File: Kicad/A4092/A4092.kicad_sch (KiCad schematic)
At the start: 0 parts

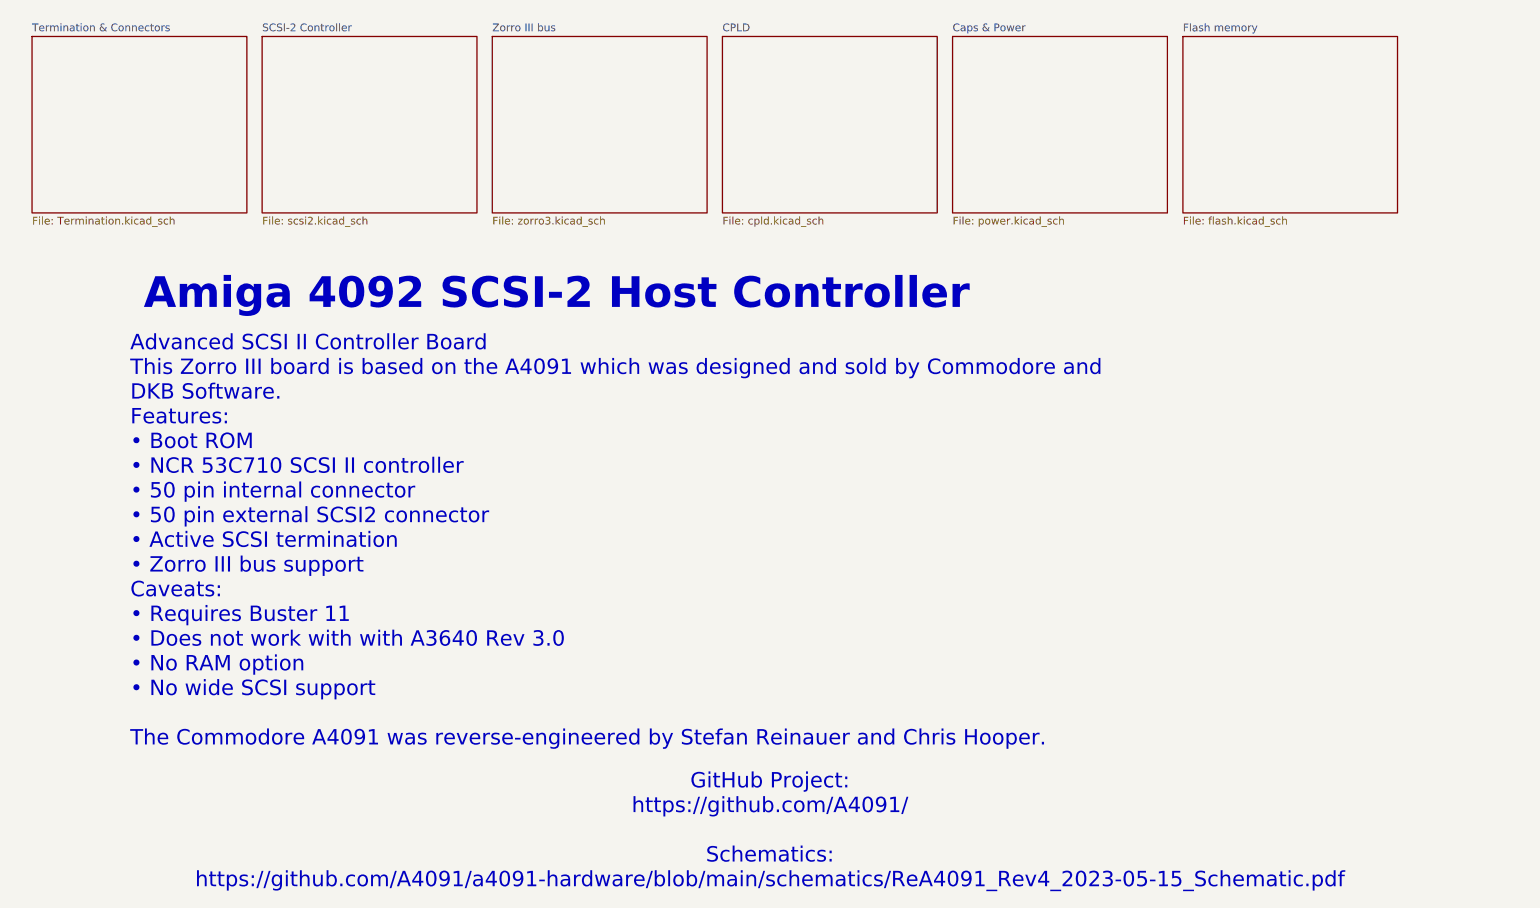
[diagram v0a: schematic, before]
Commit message: A4092 Schematics Revision C
- Power U5 / 74LVC07 from 3.3V rail
- Use ABOEH for 1OEAB on U4 / 74ABT16543
- Add bypass capacitor C501 for U5 / 74LVC07
- Remove EMI filters and capacitors from SCSI lines. They
  are a net negative for signal integrity
- Remove DIP switch circuit as all options are controlled
  by the CPLD / AutoConfig ROM now.
- Remove parallel flash memory, as SPI works reliably and
  is significantly easier to source.
- Remove all ferrite beads from signal lines, as these were
  populated with 0 Ohm resistors in all Proto devices.
- Mark power connector and 12V capacitor as DNP
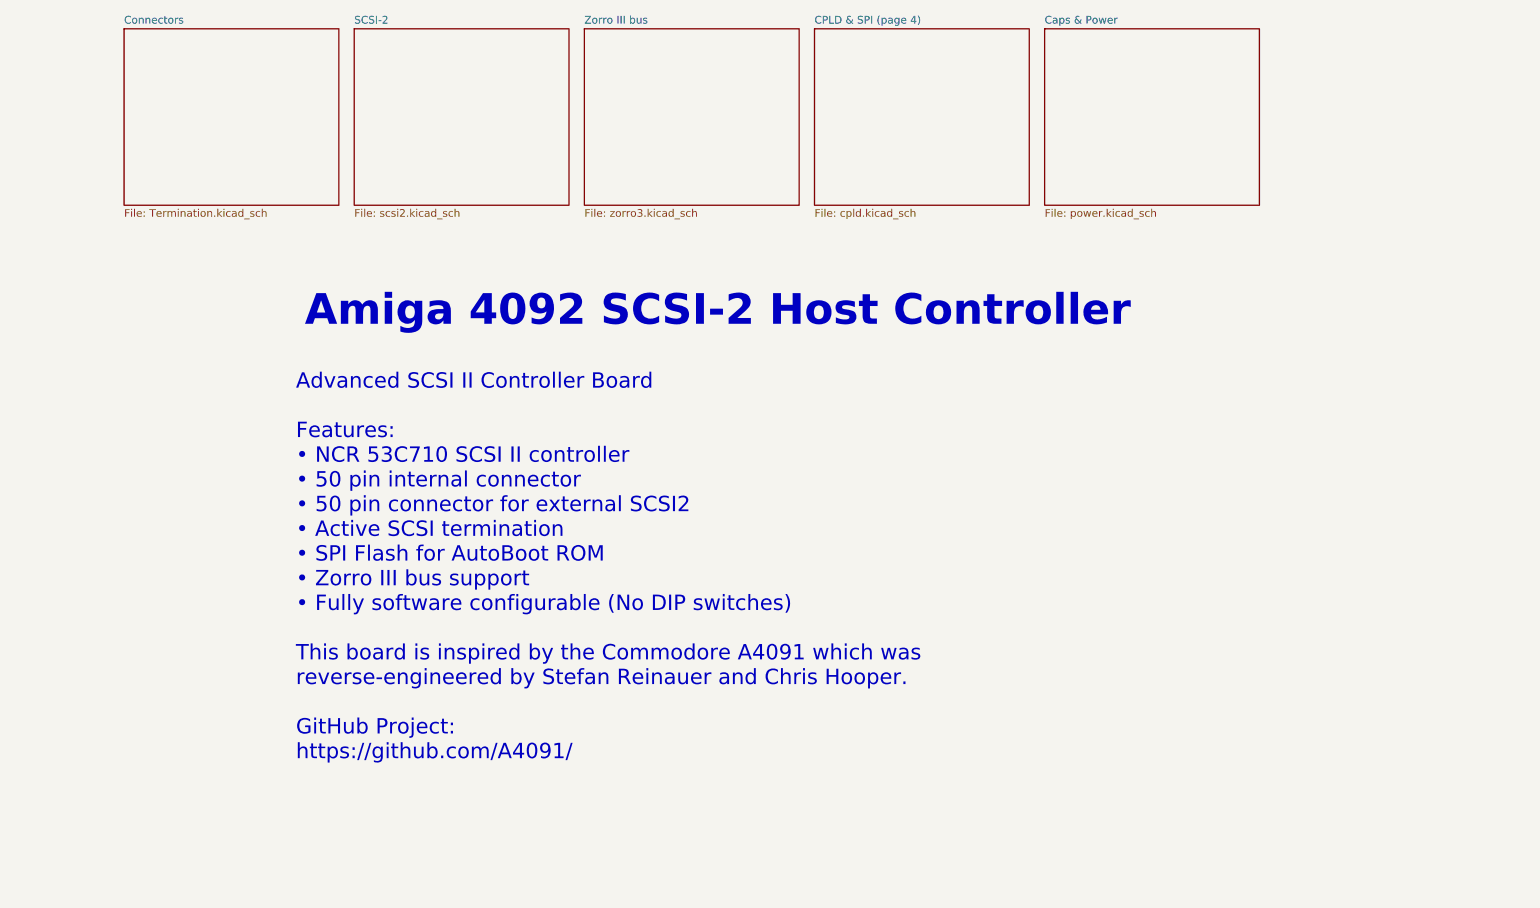
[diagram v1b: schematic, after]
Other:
- sheet CPLD renamed CPLD & SPI (page 4)
- sheet SCSI-2 Controller renamed SCSI-2
- sheet Termination & Connectors renamed Connectors
- removed sheet Flash memory
- note added: "Advanced SCSI II Controller Board Features: • NCR 53C710 SCSI II controller • 50 pin internal connector • 50 pin connector for external SCSI2 • Active SCSI termination • SPI Flash for AutoBoot ROM • Zorro III bus support • Fully software configurable (No DIP switches) This board is inspired by the Commodore A4091 which was reverse-engineered by Stefan Reinauer and Chris Hooper. GitHub Project: ht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"
- note removed: "Advanced SCSI II Controller Board This Zorro III board is based on the A4091 which was designed and sold by Commodore and DKB Software. Features: • Boot ROM • NCR 53C710 SCSI II controller • 50 pin internal connector • 50 pin external SCSI2 connector • Active SCSI termination • Zorro III bus support Caveats: • Requires Buster 11 • Does not work with with A3640 Rev 3.0 • No RAM option • No wide SC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"
- note removed: "GitHub Project: https://github.com/A4091/ Schematics: https://github.com/A4091/a4091-hardware/blob/main/schematics/ReA4091_Rev4_2023-05-15_Schematic.pdf"
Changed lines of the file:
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@@
 	(title_block
 		(title "A4092")
-		(rev "PROTO0")
+		(date "2026-01-08")
+		(rev "REV C")
 		(company "amiga.technology")
 	)
-	(text "Advanced SCSI II Controller Board\nThis Zorro III board is based on the A4091 which was designed and sold by Commodore and\nDKB Software.\nFeatures:\n• Boot ROM\n• NCR 53C710 SCSI II controller\n• 50 pin internal connector\n• 50 pin external SCSI2 connector\n• Active SCSI termination\n• Zorro III bus support\nCaveats:\n• Requires Buster 11\n• Does not work with with A3640 Rev 3.0\n• No RAM option\n• No wide SCSI support\n\nThe Commodore A4091 was reverse-engineered by Stefan Reinauer and Chris Hooper. "
-		(exclude_from_sim no)
-		(at 51.816 105.156 0)
+	(text "Advanced SCSI II Controller Board\n\nFeatures:\n• NCR 53C710 SCSI II controller\n• 50 pin internal connector\n• 50 pin connector for external SCSI2\n• Active SCSI termination\n• SPI Flash for AutoBoot ROM\n• Zorro III bus support\n• Fully software configurable (No DIP switches)\n\nThis board is inspired by the Commodore A4091 which was \nreverse-engineered by Stefan Reinauer and Chris Hooper. \n\nGitHub Project:\nhttps://github.com/A4091/"
+		(exclude_from_sim no)
+		(at 79.248 109.474 0)
 		(effects
 			(font
@@
 		)
 	)
-	(text "GitHub Project:\nhttps://github.com/A4091/\n\nSchematics:\nhttps://github.com/A4091/a4091-hardware/blob/main/schematics/ReA4091_Rev4_2023-05-15_Schematic.pdf"
-		(exclude_from_sim no)
-		(at 157.734 153.162 0)
-		(effects
-			(font
-				(size 2.54 2.54)
-			)
-		)
-	)
 	(text "Amiga 4092 SCSI-2 Host Controller\n"
 		(exclude_from_sim no)
-		(at 122.428 64.262 0)
+		(at 149.098 67.056 0)
 		(effects
 			(font
@@
 	)
 	(sheet
-		(at 187.96 21.59)
+		(at 203.2 20.32)
 		(size 35.56 29.21)
 		(exclude_from_sim no)
@@
 		)
 		(property "Sheetname" "Caps & Power"
-			(at 187.96 20.8784 0)
+			(at 203.2 19.6084 0)
 			(effects
 				(font
@@
 		)
 		(property "Sheetfile" "power.kicad_sch"
-			(at 187.96 51.3846 0)
+			(at 203.2 50.1146 0)
 			(effects
 				(font
@@
 	)
 	(sheet
-		(at 73.66 21.59)
-		(size 35.56 29.21)
-		(exclude_from_sim no)
-		(in_bom yes)
-		(on_board yes)
-		(dnp no)
-		(fields_autoplaced yes)
-		(stroke
-			(width 0.1524)
-			(type solid)
-		)
-		(fill
-			(color 0 0 0 0.0000)
-		)
-		(property "Sheetname" "SCSI-2 Controller"
-			(at 73.66 20.8784 0)
+		(at 88.9 20.32)
+		(size 35.56 29.21)
+		(exclude_from_sim no)
+		(in_bom yes)
+		(on_board yes)
+		(dnp no)
+		(fields_autoplaced yes)
+		(stroke
+			(width 0.1524)
+			(type solid)
+		)
+		(fill
+			(color 0 0 0 0.0000)
+		)
+		(property "Sheetname" "SCSI-2"
+			(at 88.9 19.6084 0)
 			(effects
 				(font
@@
 		)
 		(property "Sheetfile" "scsi2.kicad_sch"
-			(at 73.66 51.3846 0)
+			(at 88.9 50.1146 0)
 			(effects
 				(font
@@
 	)
 	(sheet
-		(at 35.56 21.59)
-		(size 35.56 29.21)
-		(exclude_from_sim no)
-		(in_bom yes)
-		(on_board yes)
-		(dnp no)
-		(fields_autoplaced yes)
-		(stroke
-			(width 0.1524)
-			(type solid)
-		)
-		(fill
-			(color 0 0 0 0.0000)
-		)
-		(property "Sheetname" "Termination & Connectors"
-			(at 35.56 20.8784 0)
+		(at 50.8 20.32)
+		(size 35.56 29.21)
+		(exclude_from_sim no)
+		(in_bom yes)
+		(on_board yes)
+		(dnp no)
+		(fields_autoplaced yes)
+		(stroke
+			(width 0.1524)
+			(type solid)
+		)
+		(fill
+			(color 0 0 0 0.0000)
+		)
+		(property "Sheetname" "Connectors"
+			(at 50.8 19.6084 0)
 			(effects
 				(font
@@
 		)
 		(property "Sheetfile" "Termination.kicad_sch"
-			(at 35.56 51.3846 0)
+			(at 50.8 50.1146 0)
 			(effects
 				(font
@@
 	)
 	(sheet
-		(at 111.76 21.59)
+		(at 127 20.32)
 		(size 35.56 29.21)
 		(exclude_from_sim no)
@@
 		)
 		(property "Sheetname" "Zorro III bus"
-			(at 111.76 20.8784 0)
+			(at 127 19.6084 0)
 			(effects
 				(font
@@
 		)
 		(property "Sheetfile" "zorro3.kicad_sch"
-			(at 111.76 51.3846 0)
+			(at 127 50.1146 0)
 			(effects
 				(font
@@
 	)
 	(sheet
-		(at 226.0914 21.5967)
-		(size 35.5286 29.2033)
-		(exclude_from_sim no)
-		(in_bom yes)
-		(on_board yes)
-		(dnp no)
-		(fields_autoplaced yes)
-		(stroke
-			(width 0.1524)
-			(type solid)
-		)
-		(fill
-			(color 0 0 0 0.0000)
-		)
-		(property "Sheetname" "Flash memory"
-			(at 226.0914 20.8851 0)
-			(effects
-				(font
-					(size 1.27 1.27)
-				)
-				(justify left bottom)
-			)
-		)
-		(property "Sheetfile" "flash.kicad_sch"
-			(at 226.0914 51.3846 0)
-			(effects
-				(font
-					(size 1.27 1.27)
-				)
-				(justify left top)
-			)
-		)
-		(instances
-			(project "A4092"
-				(path "/8f9f4021-47aa-41d9-bea7-f6ccf72098bb"
-					(page "7")
-				)
-			)
-		)
-	)
-	(sheet
-		(at 149.86 21.59)
-		(size 35.56 29.21)
-		(exclude_from_sim no)
-		(in_bom yes)
-		(on_board yes)
-		(dnp no)
-		(fields_autoplaced yes)
-		(stroke
-			(width 0.1524)
-			(type solid)
-		)
-		(fill
-			(color 0 0 0 0.0000)
-		)
-		(property "Sheetname" "CPLD"
-			(at 149.86 20.8784 0)
+		(at 165.1 20.32)
+		(size 35.56 29.21)
+		(exclude_from_sim no)
+		(in_bom yes)
+		(on_board yes)
+		(dnp no)
+		(fields_autoplaced yes)
+		(stroke
+			(width 0.1524)
+			(type solid)
+		)
+		(fill
+			(color 0 0 0 0.0000)
+		)
+		(property "Sheetname" "CPLD & SPI (page 4)"
+			(at 165.1 19.6084 0)
 			(effects
 				(font
@@
 		)
 		(property "Sheetfile" "cpld.kicad_sch"
-			(at 149.86 51.3846 0)
-			(effects
-				(font
+			(at 165.1 50.1146 0)
+			(effects
+				(font
